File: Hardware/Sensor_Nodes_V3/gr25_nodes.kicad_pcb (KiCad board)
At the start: 2 copper layers, 80 parts, among them J1 Conn_01x06_Socket, J6 Conn_01x27_Socket, J7 Conn_01x27_Socket, Q1 S9013, U1 STM32G474RBTx, U2 TPS563200, U3 MCP2542FDxMF, U4 AMS1117-3.3, U5 STM32F103C8Tx, U6 MCP2542FDxMF, Y1 8MHz

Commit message: extras
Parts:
- moved U1 1.36 mm to (119.6, 69.5)
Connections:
- C10 pad 1: XTAL_S -> Net-(U5-PD1)
- C9 pad 1: Net-(U5-PD0) -> XTAL_S
- U5 pad 5: Net-(U5-PD0) -> XTAL_S
- U5 pad 6: XTAL_S -> Net-(U5-PD1)
- Y1 pad 1: Net-(U5-PD0) -> XTAL_S
- Y1 pad 2: XTAL_S -> Net-(U5-PD1)
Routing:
- net B0: track 0.00 -> 1.57 mm

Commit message: sync update
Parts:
- removed C20: 100nF, Capacitor_SMD:C_0402_1005Metric
- C1, C2: footprint Capacitor_SMD:C_1206_3216Metric -> Capacitor_SMD:C_0603_1608Metric
- C10, C28, C29, C3, C30, C31, C9: footprint Capacitor_SMD:C_0402_1005Metric -> Capacitor_SMD:C_0603_1608Metric
- C11, C12, C13, C15, C16, C17, C18, C19, C21, C22, C23, C24, C25, C8: footprint Capacitor_SMD:C_0402_1005Metric -> Capacitor_SMD:C_0603_1608Metric; moved to B.Cu
- C4, C5: footprint Capacitor_SMD:C_0402_1005Metric -> Resistor_SMD:R_0805_2012Metric
- C6: footprint Capacitor_SMD:C_0805_2012Metric -> Capacitor_SMD:C_0603_1608Metric
- D2, D3, J6, J7, L2, Q1, R10, R13, R14, R15, R16, R17, R8, R9: moved to B.Cu
- D4, J1, U5: moved to F.Cu
- R3: footprint Resistor_SMD:R_0603_1608Metric -> Resistor_SMD:R_0402_1005Metric
- moved R28 90.5 mm to (126.2, 78.8), turned to 90 degrees
- moved R19 85.0 mm to (121.8, 62.0), turned to 180 degrees
- moved R20 84.0 mm to (121.8, 61.0), turned to 180 degrees
- moved R21 81.6 mm to (120.2, 59.5), turned to 180 degrees
- moved R25 81.5 mm to (114.0, 76.5), turned to 180 degrees
- moved R22 80.9 mm to (120.2, 58.5), turned to 180 degrees
- moved R26 80.0 mm to (114.0, 75.5), turned to 180 degrees
- moved C17 79.6 mm to (122.8, 74.0), turned to 180 degrees
- moved R23 78.9 mm to (119.0, 57.0), turned to 180 degrees
- moved R24 78.3 mm to (119.0, 56.0), turned to 180 degrees
- moved R18 77.8 mm to (114.5, 59.0), turned to -90 degrees
- moved C24 74.7 mm to (124.5, 69.2), turned to -90 degrees
- moved C19 74.5 mm to (123.5, 65.2), turned to 180 degrees
- moved C22 73.3 mm to (123.5, 66.8), turned to 180 degrees
- moved C25 72.4 mm to (123.0, 69.2), turned to -90 degrees
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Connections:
- C10 pad 1: Net-(U5-PD1) -> XTAL_S
- C11 pad 1: +3V3 -> +3.3V
- C12 pad 1: +3V3 -> +3.3V
- C13 pad 1: +3V3 -> +3.3V
- C15 pad 1: +3V3 -> +3.3V
- C16 pad 1: +3V3 -> +3.3V
- C17 pad 1: +3V3 -> +3.3V
- C18 pad 1: +3V3 -> +3.3V
- C19 pad 1: +3V3 -> +3.3V
- C21 pad 1: +3V3 -> +3.3V
- C8 pad 1: +3V3 -> +3.3V
- C9 pad 1: XTAL_S -> Net-(U5-PD0)
- Q1 pad 3: +3V3 -> +3.3V
- R8 pad 2: +3V3 -> +3.3V
- TP1 pad 1: +3V3 -> +3.3V
- U5 pad 5: XTAL_S -> Net-(U5-PD0)
- U5 pad 6: Net-(U5-PD1) -> XTAL_S
- Y1 pad 1: XTAL_S -> Net-(U5-PD0)
- Y1 pad 2: Net-(U5-PD1) -> XTAL_S
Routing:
- net GND: track 0.00 -> 30.8 mm, vias 0 -> 10
- net +12V: track 0.00 -> 22.0 mm
- net Net-(U2-SW): track 0.00 -> 9.52 mm
- net +5V: track 0.00 -> 9.47 mm, vias 0 -> 6
- net /Power/Vin_D: track 0.00 -> 9.33 mm
- net Net-(U2-VFB): track 0.00 -> 2.79 mm
- net Net-(U2-VBST): track 0.00 -> 1.81 mm
- net /Power/LED3v3: track 0.00 -> 1.64 mm
- net B0: track 1.57 -> 0.00 mm
- added copper zone on B.Cu, net (none)
- added copper zone on F.Cu, net (none)
- added copper zone on F.Cu, net +3.3V
- added copper zone on In2.Cu, net +3.3V
- added copper zone on B.Cu, net +5V
- added copper zone on F.Cu, net +5V
- added copper zone on B.Cu, net GND
- added copper zone on F.Cu, net GND
- added copper zone on In1.Cu, net GND
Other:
- copper layers 2 -> 4

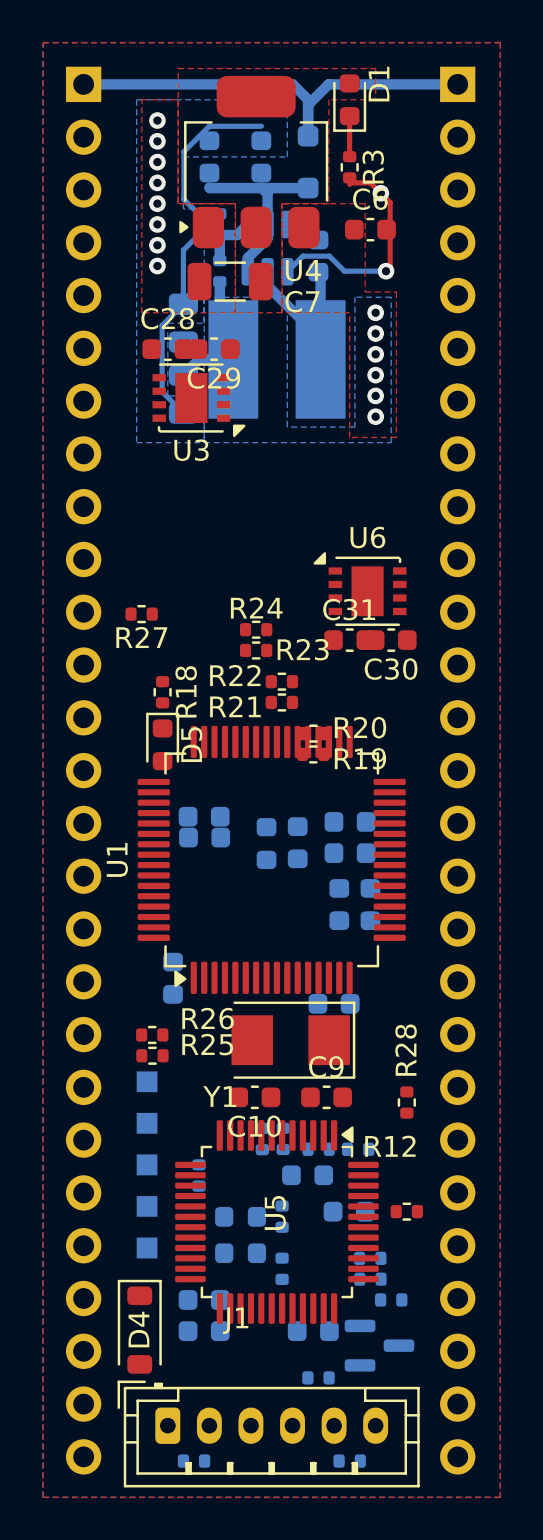
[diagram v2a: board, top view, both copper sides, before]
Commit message: finished v3, need to fix drc silkscreens
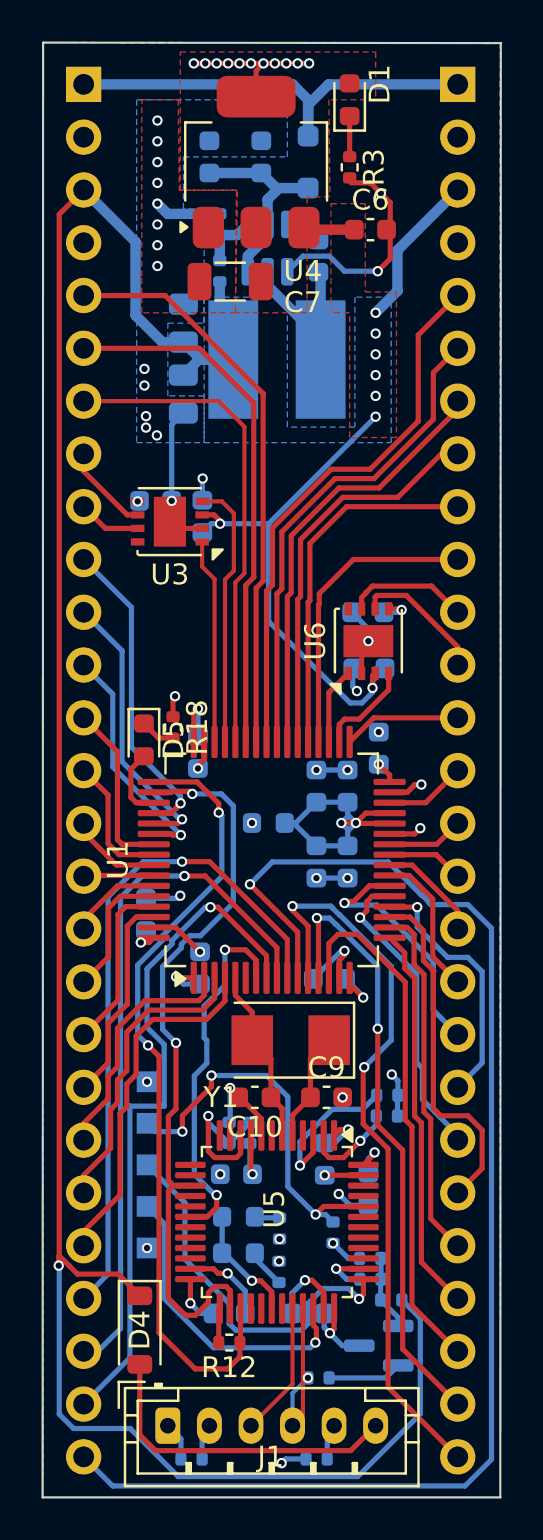
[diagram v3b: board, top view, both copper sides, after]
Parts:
- removed R19, R20, R21, R22, R23, R24, R25, R26, R27, R28: 2k2, Resistor_SMD:R_0402_1005Metric
- C28, C29, C30, C31: moved to B.Cu
- moved R12 10.6 mm to (117.7, 90.3)
- moved C15 8.92 mm to (122.3, 81.5), turned to -90 degrees
- moved C29 8.07 mm to (116.4, 50.5), turned to 90 degrees
- moved R16 7.61 mm to (115.9, 95.9)
- moved C28 7.32 mm to (114.2, 49.8)
- moved R11 7.01 mm to (122.7, 85.0), turned to -90 degrees
- moved C21 6.28 mm to (116.3, 72.3), turned to 90 degrees
- moved R6 6.09 mm to (125.3, 79.4), turned to 180 degrees
- moved U3 6.04 mm to (114.8, 50.8)
- moved R17 5.90 mm to (121.9, 95.9), turned to 180 degrees
- moved C11 5.72 mm to (118.0, 82.2)
- moved R7 5.43 mm to (125.3, 78.4), turned to 180 degrees
- moved R4 5.27 mm to (118.7, 80.2), turned to -90 degrees
- moved R5 4.38 mm to (117.7, 80.2), turned to -90 degrees
- moved C19 3.81 mm to (124.9, 61.7), turned to 90 degrees
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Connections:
- J6 pad 10: CANH2 -> PB14
- J6 pad 11: CANL2 -> CANH2
- J6 pad 12: PB15 -> CANL2
- J6 pad 7: I2C4_SCL -> I2C4_SDA
- J6 pad 8: I2C4_SDA -> I2C4_SCL
- J6 pad 9: PB14 -> PB15
- J7 pad 24: PC0 -> PC2
- J7 pad 26: PC2 -> PC0
- J7 pad 5: CANL3 -> I2C2_SDA
- J7 pad 6: CANH3 -> I2C2_SCL
- J7 pad 8: I2C2_SCL -> CANL3
- J7 pad 9: I2C2_SDA -> CANH3
- R4 pad 2: +3V3 -> +3.3V
- U1 pad 49: T_SWO -> T_DIO
- U5 pad 31: T_SWO -> unconnected-(U5-PA10-Pad31)
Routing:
- net +5V: track 9.47 -> 145.1 mm, vias 6 -> 9
- net PC3: track 0.00 -> 65.2 mm, vias 0 -> 1
- net T_DIO: track 0.00 -> 38.4 mm, vias 0 -> 2
- net T_CLK: track 0.00 -> 36.1 mm, vias 0 -> 2
- net PA0: track 0.00 -> 35.8 mm, vias 0 -> 2
- net GND: track 30.8 -> 66.1 mm, vias 10 -> 43
- net PC1: track 0.00 -> 33.8 mm, vias 0 -> 1
- net +3.3V: track 0.00 -> 33.1 mm, vias 0 -> 26
- net PC0: track 0.00 -> 33.0 mm, vias 0 -> 1
- net PC2: track 0.00 -> 32.5 mm, vias 0 -> 1
- net PA1: track 0.00 -> 29.5 mm, vias 0 -> 2
- net I2C2_SDA: track 0.00 -> 27.5 mm
- net I2C3_SDA: track 0.00 -> 26.4 mm
- net I2C2_SCL: track 0.00 -> 25.7 mm
- net PA2: track 0.00 -> 25.3 mm
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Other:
- board outline added: 22.1 x 70 mm

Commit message: DRC no error. GOOD. quick sync too.
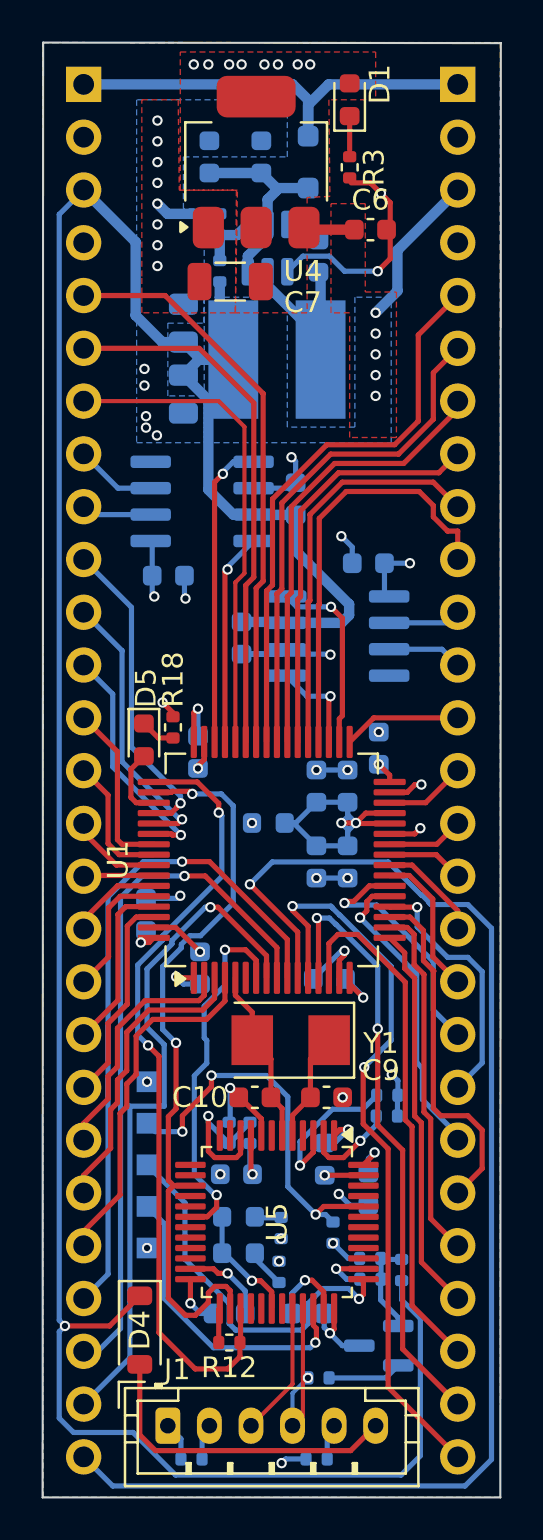
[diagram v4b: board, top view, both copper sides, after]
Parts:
- U3, U6: footprint Package_DFN_QFN:DFN-8-1EP_3x3mm_P0.65mm_EP1.55x2.4mm -> Package_SO:SOIC-8_3.9x4.9mm_P1.27mm; moved to B.Cu
- moved C31 6.30 mm to (118.3, 56.4), turned to -90 degrees
- moved C29 4.57 mm to (120.9, 49.7)
- moved C28 3.65 mm to (114.8, 53.4)
- moved C30 2.36 mm to (124.4, 52.8)
- moved U3 1.83 mm to (116.4, 49.8)
- moved R13 1.52 mm to (126.0, 86.8), turned to -90 degrees
- moved U6 1.50 mm to (122.9, 56.3), turned to 0 degrees
- moved R9 0.08 mm to (120.2, 84.8)
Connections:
- J6 pad 11: CANH2 -> CANL2
- J6 pad 12: CANL2 -> CANH2
- J7 pad 8: CANL3 -> CANH3
- J7 pad 9: CANH3 -> CANL3
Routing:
- net PB14: track 14.5 -> 20.4 mm
- net CTXD3: track 9.87 -> 14.8 mm, vias 0 -> 1
- net CRXD2: track 4.70 -> 9.15 mm, vias 0 -> 1
- net +3.3V: track 33.1 -> 29.8 mm, vias 26 -> 23
- net CANL2: track 6.48 -> 3.51 mm
- net CRXD3: track 12.9 -> 10.2 mm, vias 0 -> 1
- net CANH2: track 5.94 -> 3.61 mm
- net +5V: track 145.1 -> 143.0 mm, vias 9 -> 6
- net PB15: track 17.4 -> 19.2 mm
- net CTXD2: track 3.68 -> 4.77 mm, vias 0 -> 1
- net Net-(Q1-B): track 3.61 -> 4.63 mm
- net CANL3: track 4.30 -> 3.38 mm
- net CANH3: track 3.03 -> 3.91 mm
- net I2C4_SCL: track 19.1 -> 19.9 mm
- net I2C4_SDA: track 20.9 -> 21.7 mm
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
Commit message: finished the thing, need to optimize bom a little bit. need to flip some of the components too
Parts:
- C1, C2, C6: footprint Capacitor_SMD:C_0603_1608Metric -> Capacitor_SMD:C_0805_2012Metric
- C4, C5: footprint Resistor_SMD:R_0805_2012Metric -> Capacitor_SMD:C_0805_2012Metric
- C7: footprint Capacitor_SMD:C_1206_3216Metric -> Capacitor_SMD:C_0805_2012Metric
- D1: value LED -> RED
- L2: footprint Inductor_SMD:L_0603_1608Metric -> Capacitor_SMD:C_1206_3216Metric
- R15: value 100R -> 100
- moved L1 10.2 mm to (122.8, 33.2), turned to 0 degrees
- moved C4 9.74 mm to (122.2, 37.6), turned to 180 degrees
- moved C3 8.07 mm to (118.4, 30.8), turned to -90 degrees
- moved R1 7.38 mm to (117.0, 31.4), turned to -90 degrees
- moved D6 7.36 mm to (114.2, 34.7)
- moved C5 6.93 mm to (122.2, 39.7), turned to 180 degrees
- moved C2 6.38 mm to (117.3, 39.6), turned to 0 degrees
- moved R2 5.25 mm to (116.0, 31.4)
- moved C1 4.75 mm to (117.3, 37.6), turned to 0 degrees
- moved C7 4.53 mm to (114.4, 36.2), turned to -90 degrees
- moved U2 3.69 mm to (117.6, 34.5)
- moved L2 0.95 mm to (119.9, 64.4), turned to -90 degrees
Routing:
- net +5V: track 143.0 -> 172.0 mm, vias 6 -> 2
- net +3.3V: track 29.8 -> 43.2 mm, vias 23 -> 19
- net GND: track 66.3 -> 72.4 mm
- net +12V: track 22.0 -> 25.7 mm
- net VDDA: track 15.9 -> 17.3 mm
- net Net-(U2-SW): track 9.52 -> 8.67 mm
- net I2C2_SDA: track 27.5 -> 26.8 mm
- net I2C2_SCL: track 25.7 -> 25.2 mm
- removed copper zone on B.Cu, net +5V
- removed copper zone on F.Cu, net GND

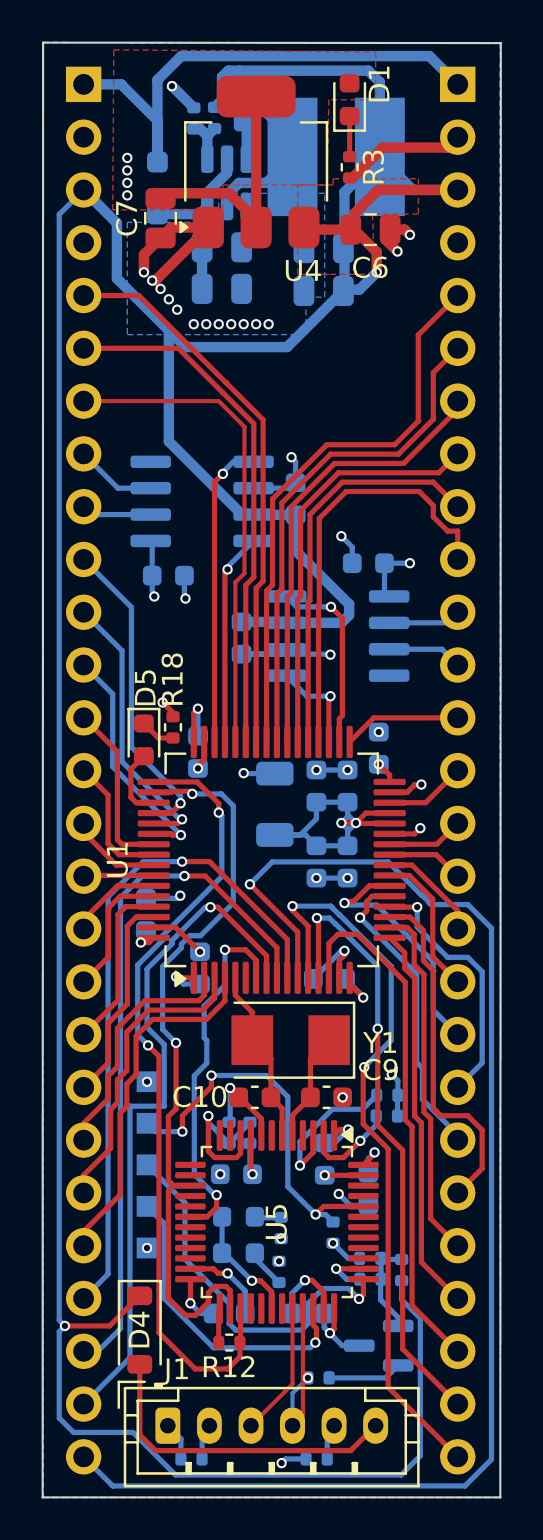
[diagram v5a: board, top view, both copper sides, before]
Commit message: alt placement made
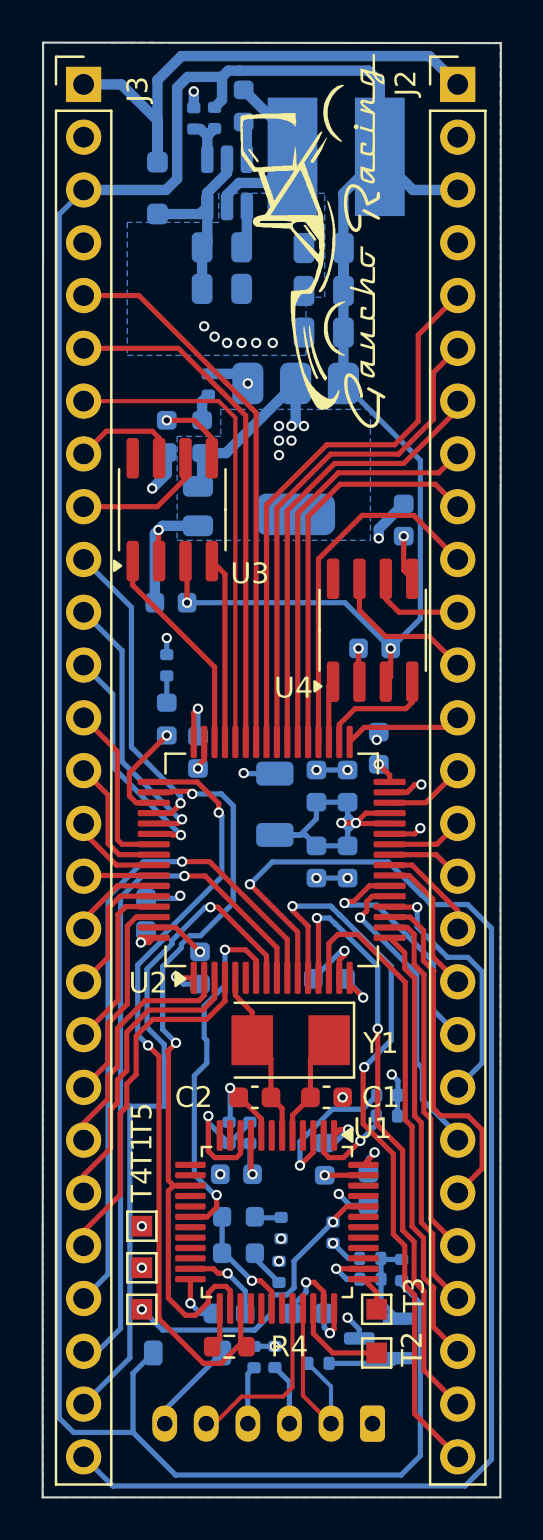
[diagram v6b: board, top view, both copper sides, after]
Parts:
- removed the R16 at (115.9, 95.9)
- removed the R17 at (121.9, 95.9)
- removed TP1: ~, TestPoint:TestPoint_Pad_1.0x1.0mm
- added G***: LOGO, LOGO, F.Cu at (121.7, 37.3)
- added R10: 5.1k, Resistor_SMD:R_0402_1005Metric, B.Cu at (119.9, 91.0)
- added R7: 5.1k, Resistor_SMD:R_0402_1005Metric, B.Cu at (118.9, 91.0)
- added T1: ~, TestPoint:TestPoint_Pad_1.0x1.0mm, F.Cu at (113.5, 86.7)
- C22: renamed from C6; moved to B.Cu
- C24: renamed from C7; moved to B.Cu
- D3: renamed from D4; moved to B.Cu
- D4: renamed from D5; moved to B.Cu
- D6: renamed from D1; footprint Diode_SMD:D_0603_1608Metric -> LED_SMD:LED_0603_1608Metric; moved to B.Cu
- J1: moved to B.Cu
- J2: renamed from J6; moved to F.Cu
- J3: renamed from J7; moved to F.Cu
- R15: renamed from R18; moved to B.Cu
- R16: renamed from R3; moved to B.Cu
- R4: renamed from R12; footprint Resistor_SMD:R_0402_1005Metric -> Resistor_SMD:R_0603_1608Metric
- T2: renamed from TP2; moved to F.Cu
- T3: renamed from TP3; moved to F.Cu
- T4: renamed from TP4; moved to F.Cu
- T5: renamed from TP5; moved to F.Cu
- U3: moved to F.Cu
- U4: renamed from U6; moved to F.Cu
- U5: renamed from U4; moved to B.Cu
- moved D6 17.7 mm to (116.4, 46.7), turned to -90 degrees
- moved C24 14.0 mm to (116.2, 50.0)
- moved U5 13.9 mm to (120.9, 47.3), turned to -90 degrees
- moved T2 13.1 mm to (124.8, 90.8), turned to 0 degrees
- moved T3 13.1 mm to (124.8, 88.7), turned to 0 degrees
- moved R16 12.5 mm to (116.7, 44.2), turned to 90 degrees
- moved C8 11.6 mm to (126.1, 50.7), turned to 90 degrees
- moved C17 11.5 mm to (114.7, 46.7), turned to -90 degrees
- moved J1 9.85 mm to (124.6, 94.2), turned to 180 degrees
- moved T4 8.95 mm to (113.5, 88.7), turned to 0 degrees
- moved C14 8.14 mm to (124.7, 56.9), turned to 180 degrees
- moved T5 6.95 mm to (113.5, 84.7), turned to 0 degrees
- moved C22 5.44 mm to (122.3, 41.7), turned to 180 degrees
- moved C20 3.80 mm to (114.9, 54.7), turned to 180 degrees
- moved R15 3.01 mm to (114.7, 57.7)
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- renumbered C9 to C1, C16 to C10, C17 to C11, C23 to C12, C18 to C13, C29 to C14, C19 to C15, C24 to C16, C30 to C17, C21 to C18, C25 to C19, C10 to C2, C31 to C20, C1 to C21, C2 to C23, C3 to C25, C4 to C26, C5 to C27, C8 to C3, C11 to C4, C12 to C5, C13 to C6, C15 to C7, C28 to C8, C22 to C9, D2 to D1, D3 to D2, D6 to D5, L2 to L1, L1 to L2, R11 to R1, R10 to R11, R13 to R12, R14 to R13, R15 to R14, R1 to R17, R2 to R18, R6 to R2, R7 to R3, R4 to R6, U5 to U1, U1 to U2, U2 to U6
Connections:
- J1 pad 2: Net-(J1-Pin_2) -> D+
- J1 pad 3: D- -> Net-(J1-Pin_3)
- J1 pad 4: D+ -> Net-(J1-Pin_4)
- J1 pad 5: Net-(J1-Pin_5) -> D-
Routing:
- net GND: track 72.4 -> 54.9 mm, vias 43 -> 36
- net CLK: track 18.3 -> 1.71 mm, vias 1 -> 0
- net VBUS: track 15.6 -> 4.54 mm
- net DIO: track 14.8 -> 4.64 mm, vias 1 -> 0
- net +5V: track 172.0 -> 163.6 mm
- net CTXD3: track 14.8 -> 10.3 mm, vias 1 -> 0
- net B0: track 18.9 -> 14.9 mm, vias 3 -> 2
- net CANH2: track 3.61 -> 7.34 mm
- net CRXD2: track 9.15 -> 5.78 mm, vias 1 -> 0
- net PB14: track 20.4 -> 17.2 mm
- net CANL3: track 3.38 -> 6.44 mm
- net Net-(J1-Pin_3): track 0.00 -> 2.99 mm
- net Net-(J1-Pin_4): track 0.00 -> 2.81 mm
- net +3.3V: track 43.2 -> 40.6 mm, vias 19 -> 22
- net D-: track 6.47 -> 8.66 mm
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- added copper zone on B.Cu, net +3.3V
- removed copper zone on F.Cu, net +3.3V
- removed copper zone on F.Cu, net +5V
